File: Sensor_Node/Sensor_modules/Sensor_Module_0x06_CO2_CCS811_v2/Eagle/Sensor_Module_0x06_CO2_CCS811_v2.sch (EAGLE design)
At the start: 30 parts, among them J1 M04_SMD_90, J2 5.5x2.1mm Barrel, J4 ARDUINO_ISP, U1 CCS811, U2 ATMEGA328P_TQFP, Y1 8MHZ

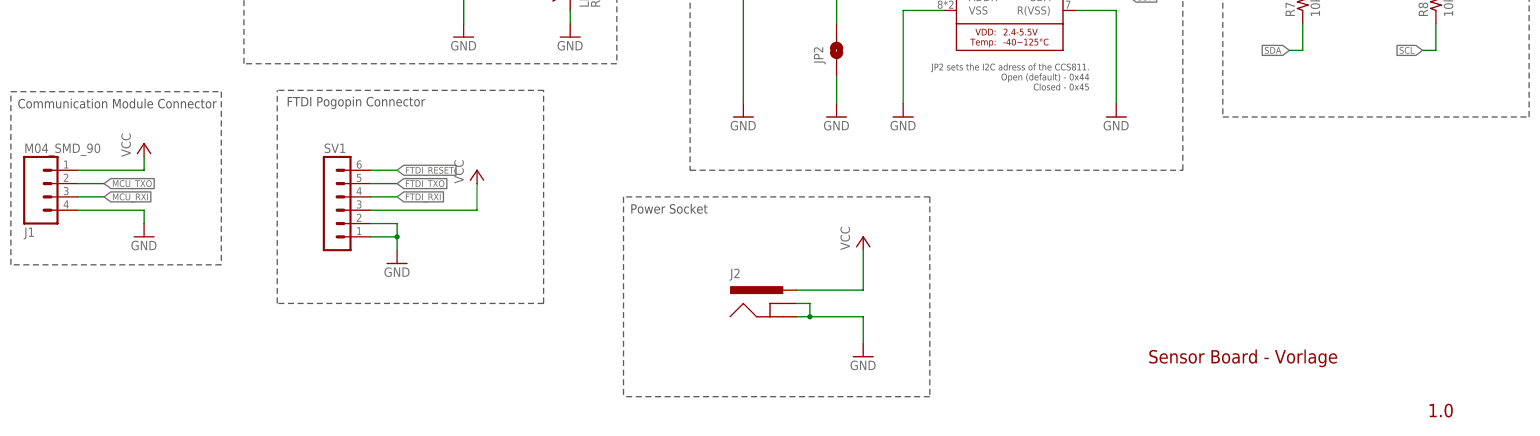
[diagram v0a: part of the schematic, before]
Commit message: Renaming boards to modules inside eagle files
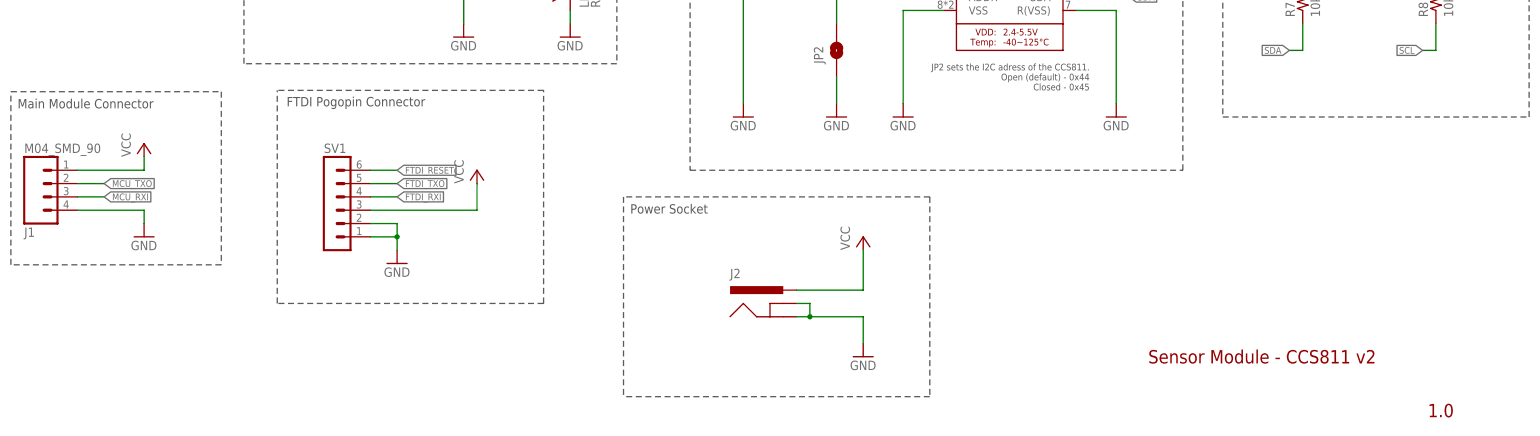
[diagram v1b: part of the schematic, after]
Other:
- note added: "Main Module Connector"
- note added: "Sensor Module - CCS811 v2"
- note removed: "Communication Module Connector"
- note removed: "Sensor Board - Vorlage"
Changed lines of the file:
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@@
 <?xml version="1.0" encoding="utf-8"?>
 <!DOCTYPE eagle SYSTEM "eagle.dtd">
-<eagle version="8.5.2">
+<eagle version="9.1.1">
 <drawing>
 <settings>
@@
 <wire x1="47.752" y1="63.246" x2="47.752" y2="30.226" width="0.1524" layer="97" style="shortdash"/>
 <wire x1="47.752" y1="30.226" x2="7.62" y2="30.226" width="0.1524" layer="97" style="shortdash"/>
-<text x="8.89" y="60.071" size="1.778" layer="97">Communication Module Connector</text>
-<text x="224.527240625" y="11.421534375" size="2.54" layer="94" font="vector">Sensor Board - Vorlage</text>
+<text x="8.89" y="60.071" size="1.778" layer="97">Main Module Connector</text>
+<text x="224.527240625" y="11.421534375" size="2.54" layer="94" font="vector">Sensor Module - CCS811 v2</text>
 <text x="277.8550125" y="1.158059375" size="2.54" layer="94" font="vector">1.0</text>
 <wire x1="109.22" y1="63.5" x2="58.42" y2="63.5" width="0.1524" layer="97" style="shortdash"/>
